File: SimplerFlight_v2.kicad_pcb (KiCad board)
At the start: 2 copper layers, 93.8 x 73.5 mm, 122 parts, among them J1 Battery 1, J10 Cam 3, J11 Servo, J12 Cam 2, J13 SWD Header, J14 DM3CS-SF, J2 Encoder, J7 Battery 2, J8 USB, J9 Cam 1, Q1 BSS816NWH6327XTSA1, Q2 NPN, Q3 BSS816NWH6327XTSA1, Q6 BSS816NWH6327XTSA1, SW1 Boot Switch, SW2 System Reset, U1 AMS1117-3.3, U2 STM32F401RETx, U3 BMP581, U4 BNO085, U5 TPS56A37RPAR, U6 TPS56A37RPAR, U7 MX25V4006EM1I-13G, Y2 Crystal

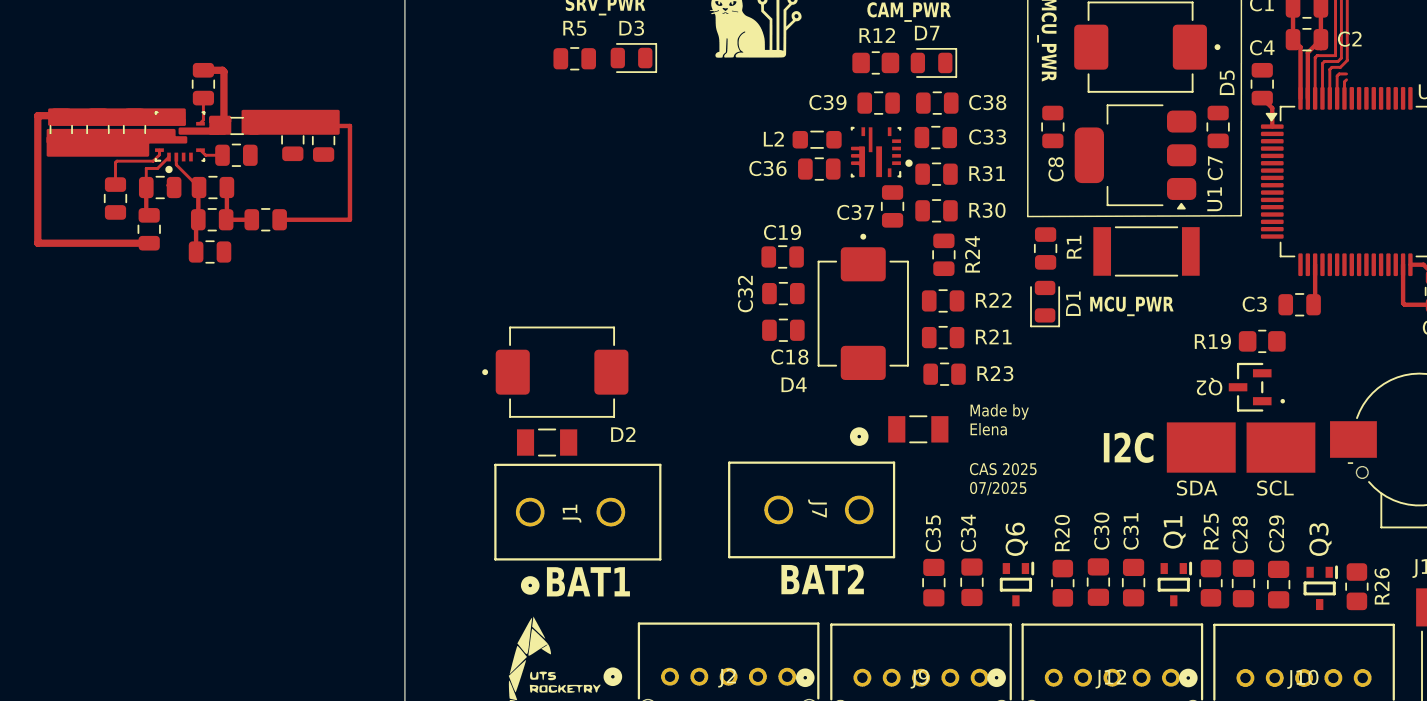
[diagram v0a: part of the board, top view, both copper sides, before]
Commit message: Routing for cam buck converter
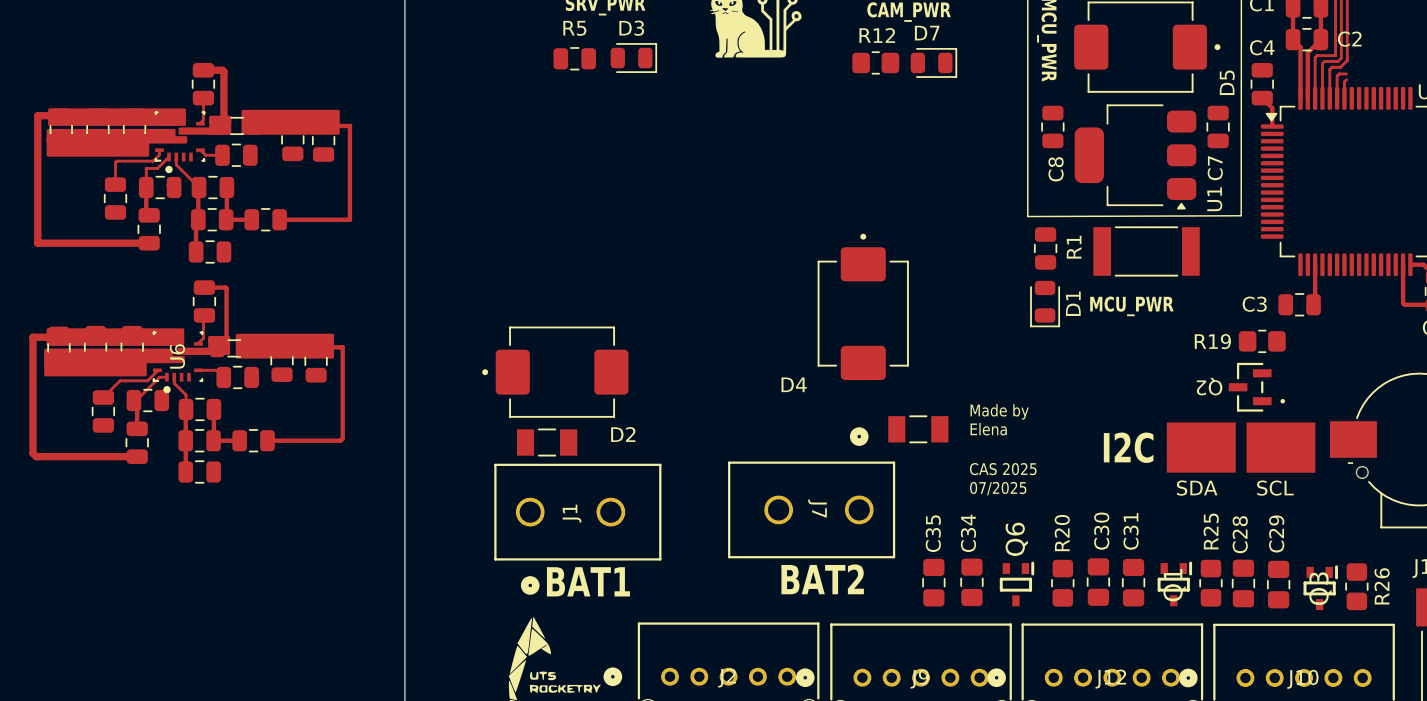
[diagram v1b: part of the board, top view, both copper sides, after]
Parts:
- moved R23 57.5 mm to (124.4, 117.8), turned to -90 degrees
- moved R21 55.5 mm to (126.7, 119.9), turned to 90 degrees
- moved R22 54.7 mm to (127.5, 117.0)
- moved R24 52.9 mm to (131.0, 121.9), turned to 0 degrees
- moved R31 52.8 mm to (131.0, 117.6)
- moved C33 50.4 mm to (133.6, 115.5)
- moved C37 49.9 mm to (131.0, 119.8), turned to 180 degrees
- moved C19 49.8 mm to (121.4, 113.4), turned to -90 degrees
- moved U6 49.6 mm to (129.5, 114.0), turned to 90 degrees
- moved R30 49.2 mm to (134.7, 119.8)
- moved C38 48.0 mm to (136.6, 114.3), turned to -90 degrees
- moved C32 47.1 mm to (123.9, 113.4), turned to -90 degrees
- moved C18 44.4 mm to (126.4, 113.4), turned to -90 degrees
- moved C36 42.9 mm to (131.3, 110.3), turned to 90 degrees
- moved L2 42.2 mm to (133.3, 113.5)
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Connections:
- net Net-(U6-BOOT) renamed /Power/BT_CAM
- net Net-(U6-MODE) renamed /Power/MODE_CAM
- net Net-(U6-SS) renamed /Power/SS_CAM
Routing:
- net /Power/VIN_CAM: track 0.00 -> 20.8 mm
- net /Power/5V_CAM: track 0.00 -> 13.2 mm
- net /Power/FB_CAM_PWR: track 0.00 -> 6.81 mm
- net /Power/SW_CAM_PWR: track 0.00 -> 5.68 mm
- net /Power/EN_CAM_PWR: track 0.00 -> 4.94 mm
- net /Power/MODE_CAM: track 0.00 -> 4.49 mm
- net Net-(C37-Pad1): track 0.00 -> 3.92 mm
- net /Power/BT_CAM: track 0.00 -> 2.07 mm
- net /Power/SS_CAM: track 0.00 -> 1.93 mm

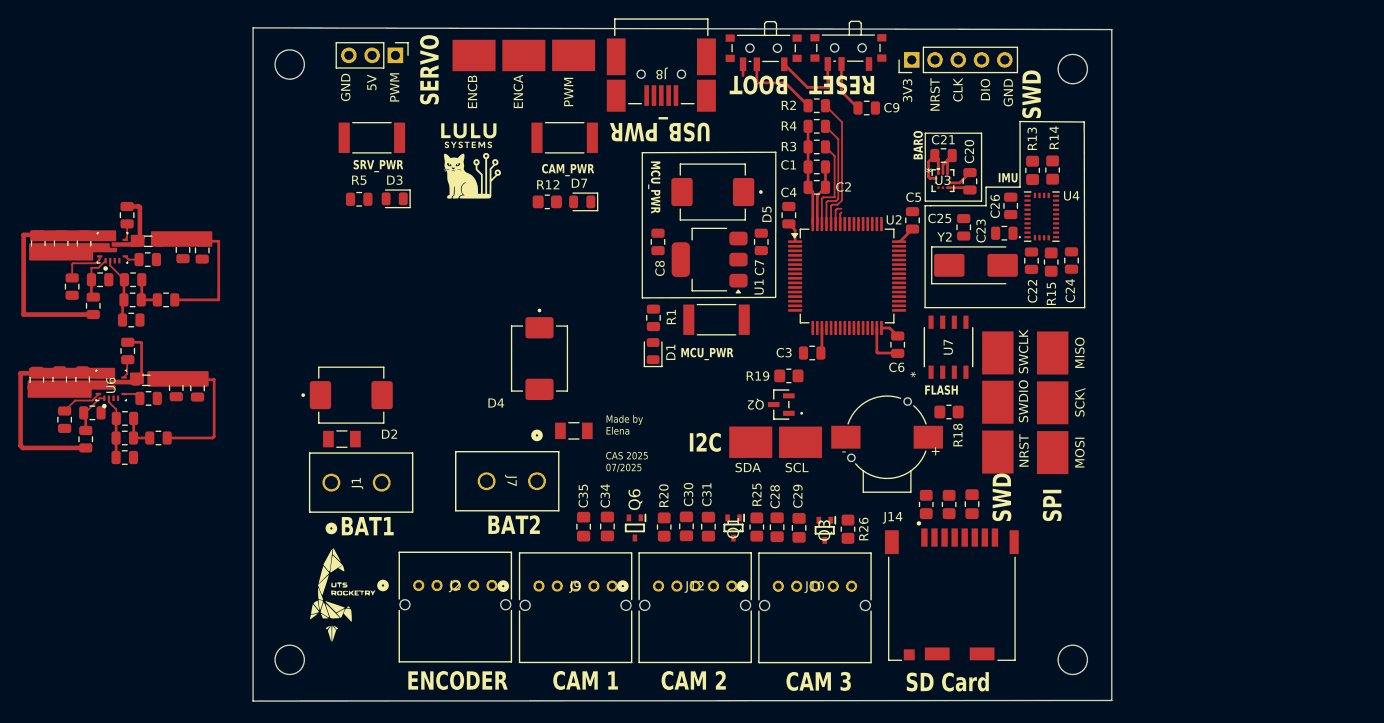
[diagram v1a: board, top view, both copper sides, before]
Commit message: Routes for power
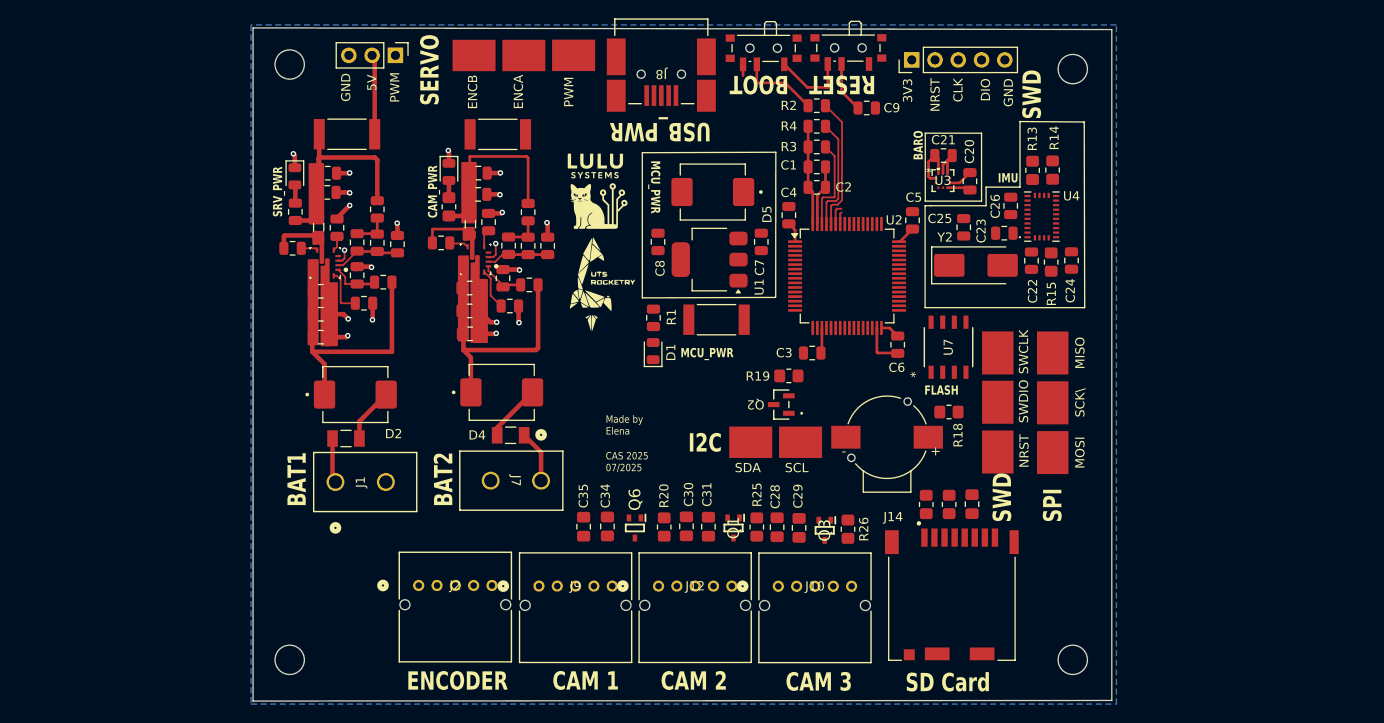
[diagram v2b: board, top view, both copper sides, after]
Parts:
- moved R24 51.6 mm to (177.2, 98.8), turned to 90 degrees
- moved R21 51.3 mm to (175.2, 103.1), turned to 180 degrees
- moved R23 50.2 mm to (173.0, 105.4), turned to 0 degrees
- moved C37 48.8 mm to (175.0, 98.8), turned to -90 degrees
- moved C19 47.6 mm to (168.7, 108.4), turned to 0 degrees
- moved R30 47.3 mm to (175.0, 95.1), turned to -90 degrees
- moved R22 47.2 mm to (172.3, 102.3), turned to 90 degrees
- moved R31 45.9 mm to (172.9, 98.8), turned to -90 degrees
- moved C32 45.4 mm to (168.6, 105.9), turned to 0 degrees
- moved G*** 44.2 mm to (181.9, 103.1)
- moved C18 43.4 mm to (168.6, 103.4), turned to 0 degrees
- moved U6 42.1 mm to (169.3, 100.3), turned to 180 degrees
- moved C33 41.8 mm to (170.7, 96.2), turned to 90 degrees
- moved L2 39.3 mm to (168.7, 96.4), turned to 90 degrees
- moved C38 39.2 mm to (169.6, 93.2), turned to 0 degrees
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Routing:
- net GND: track 27.4 -> 62.5 mm, vias 0 -> 20
- net /Peripherals/5V_SERVO: track 0.00 -> 8.73 mm
- net /Power/5V_SERVO: track 15.1 -> 21.7 mm
- net /Power/BAT2: track 0.00 -> 6.28 mm
- net /Power/BAT_1: track 0.00 -> 6.01 mm
- net Net-(F2-Pad1): track 0.00 -> 5.72 mm
- net /Power/VIN_SERVO: track 17.9 -> 23.1 mm
- net /Power/VIN_CAM: track 20.8 -> 25.7 mm
- net Net-(F1-Pad1): track 0.00 -> 4.88 mm
- net /Power/5V_CAM: track 13.2 -> 15.7 mm
- net Net-(D3-A): track 0.00 -> 2.01 mm
- net Net-(D7-A): track 0.00 -> 1.87 mm
- added copper zone on B.Cu, net GND

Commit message: More routing - sync
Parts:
- moved C37 1.56 mm to (176.6, 98.9)
- moved C39 1.56 mm to (171.2, 91.0)
- moved R21 1.56 mm to (176.7, 103.2)
- moved R22 1.56 mm to (173.8, 102.4)
- moved R23 1.56 mm to (174.6, 105.5)
- moved R24 1.56 mm to (178.7, 98.9)
- moved R30 1.56 mm to (176.6, 95.2)
- moved C19 1.56 mm to (170.3, 108.5)
- moved D4 1.56 mm to (173.7, 114.9)
- moved D7 1.56 mm to (167.9, 90.8)
- moved F2 1.56 mm to (174.7, 119.6)
- moved R12 1.56 mm to (167.9, 94.6)
- moved R31 1.56 mm to (174.5, 98.9)
- moved C33 1.56 mm to (172.3, 96.3)
- moved C38 1.56 mm to (171.1, 93.3)
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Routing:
- net /Peripherals/5V_CAM: track 0.00 -> 108.2 mm
- net /Peripherals/5V_SERVO: track 8.73 -> 61.0 mm
- net /Power/VIN_CAM: track 25.7 -> 44.1 mm
- net /Power/VBUS_MCU: track 0.00 -> 8.04 mm

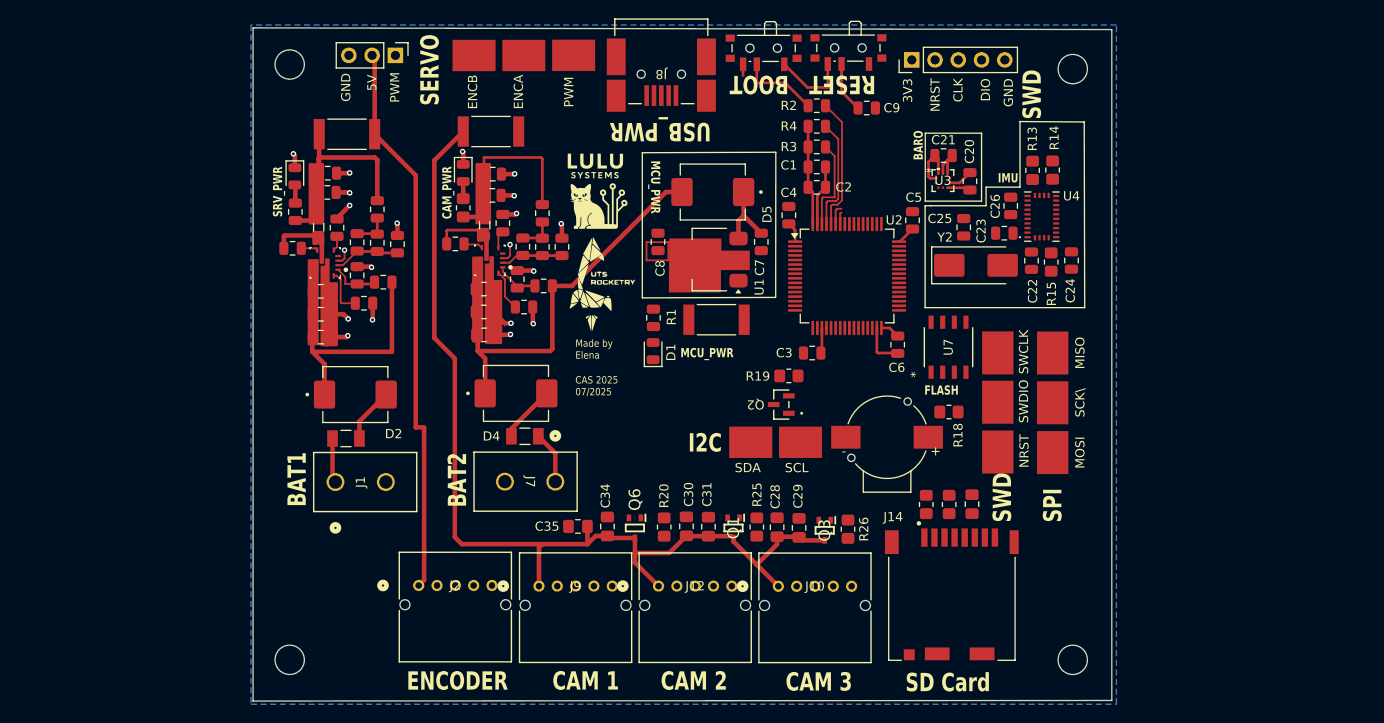
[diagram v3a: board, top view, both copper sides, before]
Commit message: Re-arranged sensor, storage and peripheral component layout
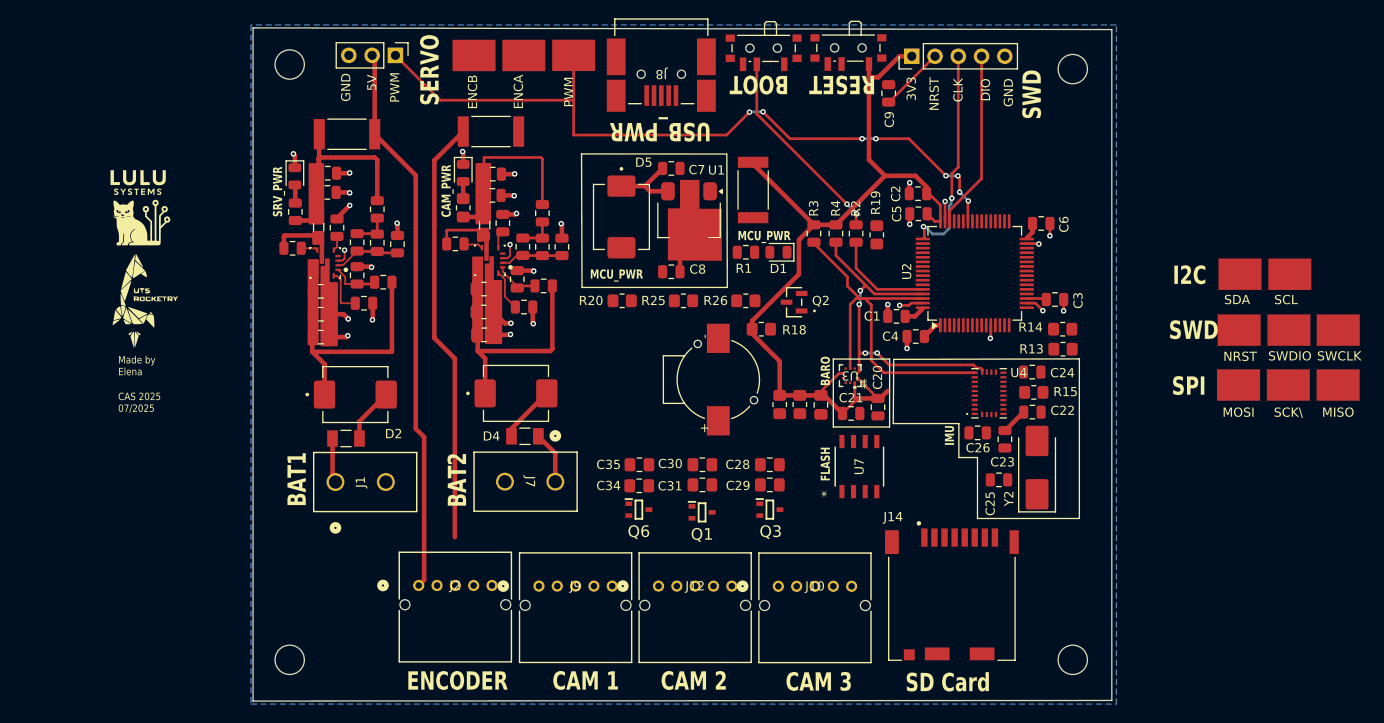
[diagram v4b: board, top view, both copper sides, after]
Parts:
- moved SDA 56.5 mm to (252.8, 101.9)
- moved SCL 56.5 mm to (258.2, 101.9)
- moved G*** 50.0 mm to (132.4, 94.6)
- moved G*** 50.0 mm to (131.9, 104.9)
- moved SWCLK 37.3 mm to (263.5, 108.0), turned to 180 degrees
- moved SWDIO 32.7 mm to (258.1, 108.0), turned to 180 degrees
- moved MISO 31.4 mm to (263.5, 114.0), turned to 180 degrees
- moved C21 29.9 mm to (210.3, 117.1)
- moved NRST 29.5 mm to (252.7, 108.0), turned to 0 degrees
- moved C25 27.8 mm to (226.4, 124.4), turned to 180 degrees
- moved R26 27.3 mm to (198.8, 104.8), turned to 180 degrees
- moved C3 27.1 mm to (232.6, 104.7), turned to 0 degrees
- moved C20 26.6 mm to (213.2, 116.4)
- moved R25 26.0 mm to (192.0, 104.8), turned to 180 degrees
- moved SCK\ 25.8 mm to (258.0, 114.0), turned to 180 degrees
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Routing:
- net /Microcontroller/SERVO_PWM: track 0.00 -> 81.6 mm, vias 0 -> 8
- net /Headers/+3V3: track 29.6 -> 106.2 mm
- net /Peripherals/5V_CAM: track 108.2 -> 46.5 mm
- net /Microcontroller/12C1_SDA: track 10.1 -> 42.3 mm
- net /Microcontroller/12C1_SCL: track 12.3 -> 37.2 mm, vias 0 -> 4
- net /Microcontroller/SYS_JTCK-SWCLK: track 0.00 -> 24.3 mm, vias 0 -> 2
- net /Microcontroller/SYS_JTMS-SWDIO: track 0.00 -> 19.5 mm
- net /Power/VIN_CAM: track 44.1 -> 25.7 mm
- net /Microcontroller/SW_BOOT0: track 8.66 -> 22.1 mm, vias 0 -> 2
- net GND: track 62.5 -> 53.0 mm, vias 20 -> 31
- net /Microcontroller/BOOT0: track 14.5 -> 11.1 mm
- net /Power/3V3: track 0.00 -> 3.38 mm
- net /Microcontroller/USART1_RX: track 2.23 -> 0.00 mm
- net NRST: track 5.55 -> 7.13 mm
- net /Microcontroller/USART1_TX: track 1.33 -> 0.00 mm
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
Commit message: more routing
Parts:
- moved R20 16.7 mm to (201.9, 103.0)
- moved Y2 12.6 mm to (218.7, 118.9), turned to -90 degrees
- moved R25 10.0 mm to (202.0, 105.0)
- moved C25 9.65 mm to (222.0, 115.8), turned to 90 degrees
- moved R15 8.45 mm to (231.6, 123.2), turned to 180 degrees
- moved G*** 7.46 mm to (139.8, 95.2)
- moved G*** 7.46 mm to (139.4, 105.5)
- moved C24 6.77 mm to (232.5, 118.9), turned to -90 degrees
- moved C22 6.67 mm to (227.8, 123.2), turned to 180 degrees
- moved U4 4.87 mm to (228.5, 118.7)
- moved C20 4.44 mm to (210.1, 113.3), turned to 90 degrees
- moved R18 4.39 mm to (201.4, 112.2)
- moved Q2 4.31 mm to (205.1, 109.1)
- moved R26 3.97 mm to (202.0, 107.2)
- moved C23 3.62 mm to (224.2, 122.1)
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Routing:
- net /Headers/+3V3: track 106.2 -> 202.2 mm
- net /Microcontroller/SERVO_PWM: track 81.6 -> 0.00 mm, vias 8 -> 0
- net /Microcontroller/SW_BOOT0: track 22.1 -> 0.00 mm, vias 2 -> 0
- net /Microcontroller/CAM_3_EN: track 0.00 -> 18.3 mm, vias 0 -> 6
- net /Microcontroller/CAM_2_EN: track 0.00 -> 17.7 mm, vias 0 -> 6
- net /Microcontroller/CAM_1_EN: track 0.00 -> 17.3 mm, vias 0 -> 6
- net Net-(U4-ENV_SDA): track 0.00 -> 9.93 mm
- net Net-(U4-XOUT32/CLKSEL1): track 0.00 -> 9.65 mm
- net Net-(U4-XIN32): track 0.00 -> 9.06 mm
- net Net-(U4-ENV_SCL): track 0.00 -> 7.55 mm
- net NRST: track 7.13 -> 0.00 mm
- net GND: track 53.0 -> 46.8 mm, vias 31 -> 26
- net /Microcontroller/BUZZ: track 0.00 -> 5.83 mm
- net Net-(U4-~{BOOT}): track 0.00 -> 5.01 mm
- net /Microcontroller/12C1_SCL: track 37.2 -> 41.1 mm
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
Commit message: Sync
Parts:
- removed C28, C31, C35: 10uF, Capacitor_SMD:C_0805_2012Metric_Pad1.18x1.45mm_HandSolder
- removed C29, C30, C34: 100uF, Capacitor_SMD:C_0805_2012Metric_Pad1.18x1.45mm_HandSolder
- removed MOSI, SCK\: 5016, 5016:KEYSTONE_5016
- added MOSI : 5016, 5016:KEYSTONE_5016, F.Cu at (235.8, 131.2)
- added SCK: 5016, 5016:KEYSTONE_5016, F.Cu at (227.7, 116.6)
- moved ENCB 59.9 mm to (149.1, 134.4), turned to 0 degrees
- moved ENCA 59.7 mm to (154.9, 134.4), turned to 0 degrees
- moved SWCLK 56.7 mm to (210.9, 86.7), turned to 90 degrees
- moved SWDIO 46.7 mm to (216.5, 86.8), turned to 90 degrees
- moved NRST 32.7 mm to (227.8, 86.7), turned to 90 degrees
- moved MISO 30.0 mm to (235.8, 125.6), turned to 90 degrees
- moved G*** 26.4 mm to (164.5, 104.8)
- moved G*** 26.4 mm to (163.6, 115.8)
- moved R26 21.6 mm to (192.7, 126.7)
- moved R13 20.9 mm to (212.9, 114.3), turned to -90 degrees
- moved R25 20.8 mm to (192.7, 123.6)
- moved R20 19.6 mm to (192.7, 120.3)
- moved R14 18.1 mm to (215.1, 114.3), turned to -90 degrees
- moved Q3 16.2 mm to (185.2, 126.8), turned to 180 degrees
- moved U4 13.7 mm to (214.8, 119.5), turned to 180 degrees
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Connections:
- J10 pad 1: /Peripherals/5V_CAM -> /Peripherals/CAM_3_VO
- J10 pad 5: unconnected-(J10-Pad5) -> GND
- J12 pad 1: /Peripherals/5V_CAM -> /Peripherals/CAM_2_VO
- J12 pad 5: unconnected-(J12-Pad5) -> GND
- J9 pad 1: /Peripherals/5V_CAM -> /Peripherals/CAM_1_VO
- J9 pad 5: unconnected-(J9-Pad5) -> GND
- Q1 pad 2: GND -> /Peripherals/CAM_2_VO
- Q3 pad 2: GND -> /Peripherals/CAM_3_VO
- Q6 pad 2: GND -> /Peripherals/CAM_1_VO
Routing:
- net /Microcontroller/SD_MEM_CS: track 0.00 -> 67.4 mm, vias 0 -> 6
- net GND: track 46.8 -> 107.8 mm, vias 26 -> 55
- net /Microcontroller/SPI1_MOSI: track 0.00 -> 55.5 mm, vias 0 -> 8
- net /Headers/+3V3: track 202.2 -> 248.1 mm
- net /Microcontroller/SPI1_MISO: track 0.00 -> 45.1 mm, vias 0 -> 6
- net /Microcontroller/SPI1_SCK: track 0.00 -> 40.8 mm, vias 0 -> 4
- net NRST: track 0.00 -> 32.0 mm, vias 0 -> 4
- net /Microcontroller/ENC_B: track 0.00 -> 29.1 mm
- net /Peripherals/5V_CAM: track 46.5 -> 74.8 mm
- net /Microcontroller/CAM_3_EN: track 18.3 -> 45.6 mm, vias 6 -> 4
- net /Peripherals/CAM_1_VO: track 0.00 -> 25.0 mm, vias 0 -> 2
- net /Microcontroller/CAM_2_EN: track 17.7 -> 42.7 mm, vias 6 -> 4
- net Net-(Q2-B): track 0.00 -> 23.8 mm, vias 0 -> 2
- net /Microcontroller/SW_BOOT0: track 0.00 -> 23.1 mm, vias 0 -> 6
- net /Peripherals/CAM_3_VO: track 0.00 -> 22.6 mm, vias 0 -> 2
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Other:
- board text added: "SWCLK"
- board text added: "SWDIO"
- board text removed: "CLK"
- board text removed: "DIO"
- board text removed: "I2C"
- board text removed: "SPI"
